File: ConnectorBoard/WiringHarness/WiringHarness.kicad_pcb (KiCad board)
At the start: 2 copper layers, 55 x 30 mm, 16 parts, among them J1 Barrel_Jack, J2 Conn_01x03, J3 Conn_01x03, J4 Conn_02x05_Odd_Even, U1 L7805, U2 L7805

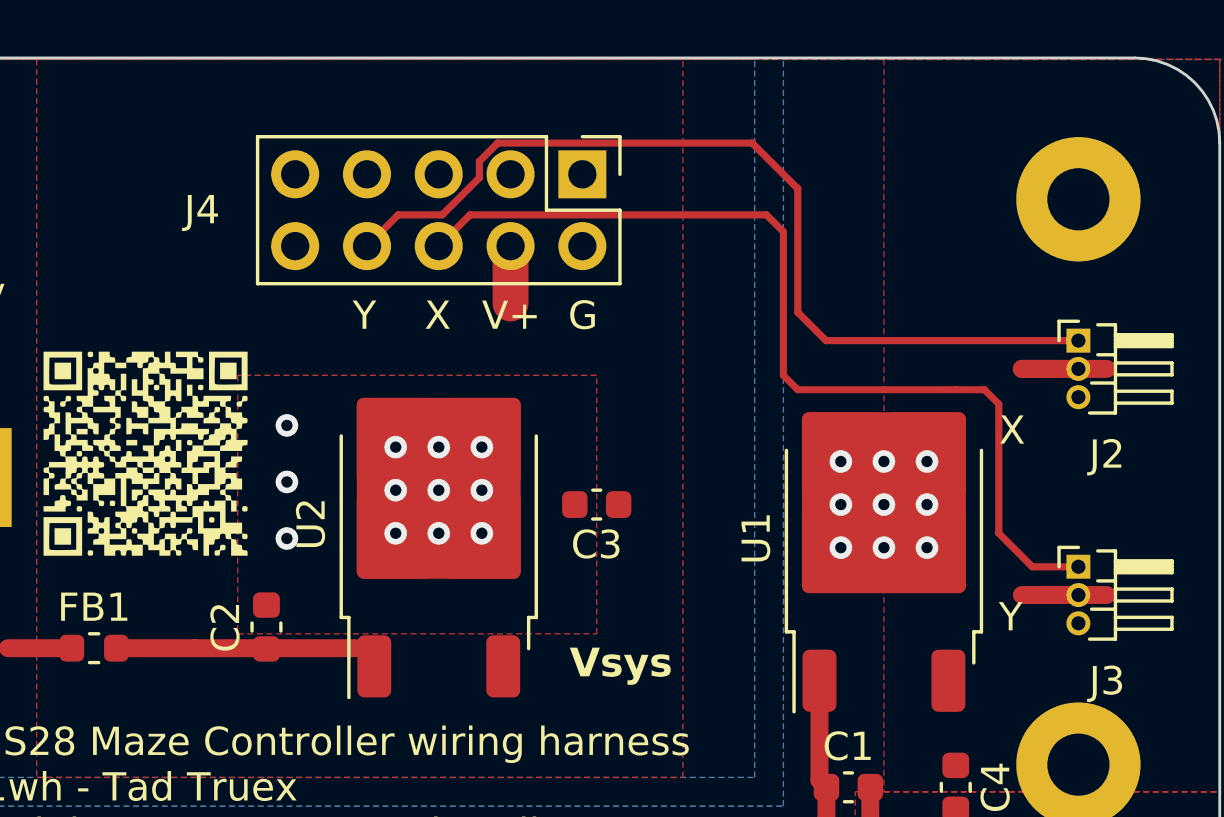
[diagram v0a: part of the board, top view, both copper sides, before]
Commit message: Tweak the connector board a bit.  Rearrange X and Y.  May do more depending on the other board.
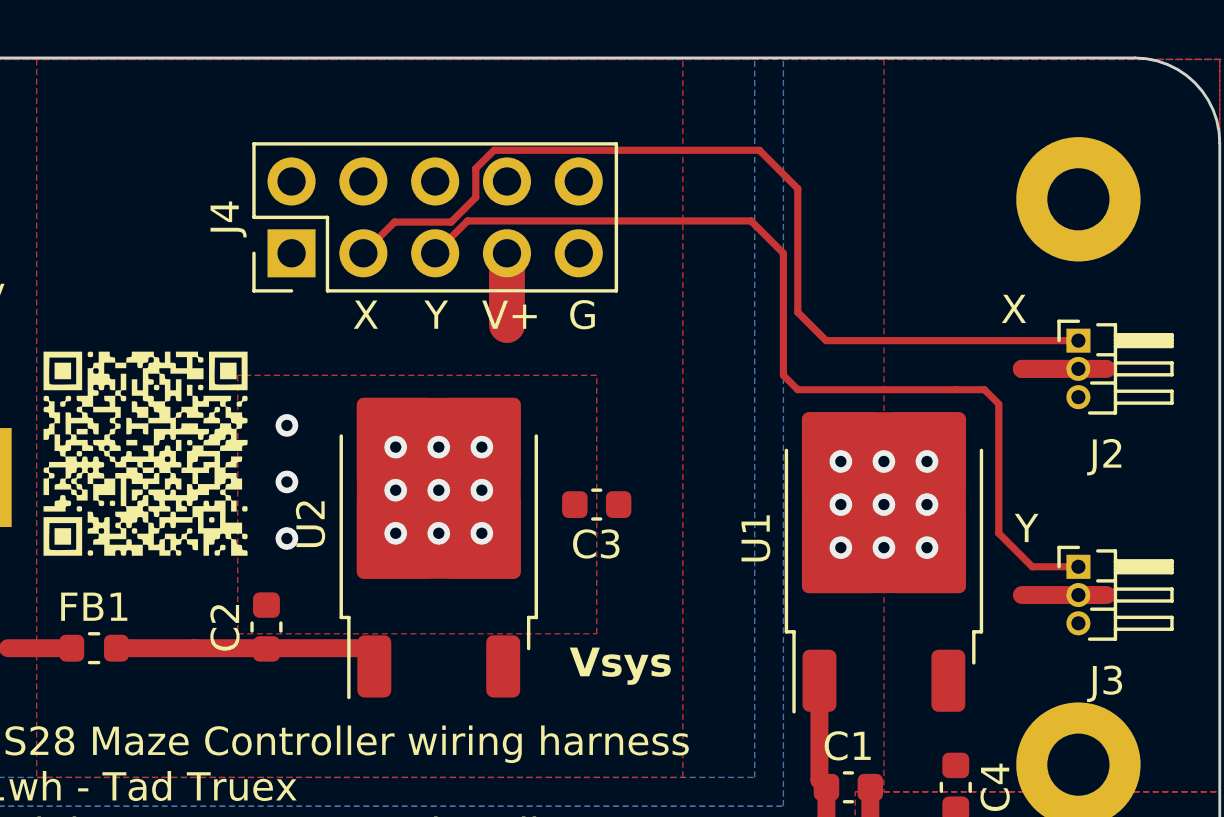
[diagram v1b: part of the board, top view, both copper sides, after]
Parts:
- moved J4 10.7 mm to (177.2, 41.9), turned to 90 degrees
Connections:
- J2 pad 1: /ServoY -> /ServoX
- J3 pad 1: /ServoX -> /ServoY
- J4 pad 2: GND -> unconnected-(J4-Pin_2-Pad2)
- J4 pad 3: unconnected-(J4-Pin_3-Pad3) -> /ServoX
- J4 pad 4: /Vsys -> unconnected-(J4-Pin_4-Pad4)
- J4 pad 5: unconnected-(J4-Pin_5-Pad5) -> /ServoY
- J4 pad 6: /ServoX -> unconnected-(J4-Pin_6-Pad6)
- J4 pad 7: unconnected-(J4-Pin_7-Pad7) -> /Vsys
- J4 pad 8: /ServoY -> unconnected-(J4-Pin_8-Pad8)
- J4 pad 9: unconnected-(J4-Pin_9-Pad9) -> GND
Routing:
- net /ServoX: track 33.9 -> 32.8 mm
- net /ServoY: track 32.5 -> 33.5 mm
- net /Vsys: track 2.03 -> 2.54 mm

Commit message: updates to connector
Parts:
- removed FB1: FerriteBead_Small, Inductor_SMD:L_0603_1608Metric
- removed G***: LOGO, QRCodeLibrary:v0.1wh
- added C5: 1uF, Capacitor_SMD:C_0603_1608Metric, F.Cu at (191.5, 43.0)
- added C6: 1uF, Capacitor_SMD:C_0603_1608Metric, F.Cu at (190.7, 37.0)
- added D1: D_Schottky, Diode_SMD:D_SMA, F.Cu at (170.0, 39.2)
- added J5: Socket, Connector_PinSocket_2.54mm:PinSocket_1x04_P2.54mm_Vertical, F.Cu at (184.6, 28.8)
- added J6: Qwiic, Connector_JST:JST_SH_SM04B-SRSS-TB_1x04-1MP_P1.00mm_Horizontal, F.Cu at (197.0, 32.9)
- added JP1: SolderJumper_3_Bridged12, Jumper:SolderJumper-3_P1.3mm_Bridged12_RoundedPad1.0x1.5mm, F.Cu at (197.3, 39.0)
- J2, J3: footprint Connector_PinHeader_1.00mm:PinHeader_1x03_P1.00mm_Horizontal -> Connector_PinHeader_2.54mm:PinHeader_1x03_P2.54mm_Horizontal
- U2: value L7805 -> TLV75533PDBV; footprint Package_TO_SOT_SMD:TO-252-2 -> Package_TO_SOT_SMD:SOT-23-5
- moved J4 19.5 mm to (187.4, 58.5), turned to -90 degrees
- moved U2 14.2 mm to (190.8, 40.0), turned to 0 degrees
- moved C2 9.81 mm to (186.1, 55.9), turned to 0 degrees
- moved H1 5.00 mm to (205.0, 35.0)
- moved H5 5.00 mm to (160.0, 35.0)
- moved J2 5.00 mm to (205.0, 40.0)
- moved J3 3.00 mm to (205.0, 50.0)
- moved C3 2.79 mm to (185.9, 52.7), turned to 0 degrees
- moved C4 0.66 mm to (200.0, 60.8)
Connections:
- C2 pad 1: /Visol -> /Vsys
- J4 pad 2: unconnected-(J4-Pin_2-Pad2) -> /SCL
- J4 pad 4: unconnected-(J4-Pin_4-Pad4) -> /SDA
- U2 pad 1: /Visol -> /VoutServo
- U2 pad 3: /Vsys -> /VoutServo
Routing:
- net /ServoY: track 33.5 -> 0.00 mm
- net /ServoX: track 32.8 -> 0.00 mm
- net /Visol: track 9.39 -> 0.00 mm
- net /VoutServo: track 8.00 -> 0.00 mm
- net Net-(J6-Pin_2): track 0.00 -> 4.21 mm
- net Net-(JP1-B): track 0.00 -> 4.13 mm
- net GND: track 4.23 -> 7.26 mm, vias 25 -> 4
- net /Vsys: track 2.54 -> 0.20 mm
- net +12V: track 8.03 -> 9.39 mm
- removed copper zone on F.Cu, net +12V
- removed copper zone on F.Cu, net /Vsys
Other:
- board size 55 x 30 mm -> 55 x 35 mm

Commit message: decent candidate for rev 0.5wh
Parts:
- added G***: LOGO, QRCodeLibrary:v0.5wh, F.Cu at (168.5, 60.0)
- added J7: Header, Connector_PinHeader_2.54mm:PinHeader_1x04_P2.54mm_Horizontal, F.Cu at (166.0, 30.0)
- moved C1 14.6 mm to (190.2, 47.8)
- moved C3 13.9 mm to (172.5, 56.5)
- moved C2 13.6 mm to (172.5, 54.2)
- moved D1 11.1 mm to (172.8, 50.0)
- moved C6 6.35 mm to (197.0, 38.0), turned to 0 degrees
- moved H1 5.00 mm to (205.0, 30.0)
- moved H5 5.00 mm to (160.0, 30.0)
- moved J6 4.88 mm to (197.0, 28.0)
- moved C5 3.50 mm to (191.5, 39.5)
- moved JP1 3.50 mm to (197.3, 35.5)
- moved U2 3.50 mm to (190.8, 36.5)
- moved C4 3.09 mm to (198.2, 58.2), turned to 180 degrees
- moved U1 2.65 mm to (196.7, 49.7)
- moved J2 2.52 mm to (205.0, 37.5)
- moved J3 2.52 mm to (205.0, 47.5)
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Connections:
- C1 pad 1: +12V -> /Vsys
- D1 pad 2: +12V -> Net-(D1-A)
- J1 pad 1: +12V -> Net-(D1-A)
- J4 pad 1: unconnected-(J4-Pin_1-Pad1) -> /ServoX
- J4 pad 2: /SCL -> /ServoY
- J4 pad 3: /ServoX -> /SCL
- J4 pad 5: /ServoY -> /D0
- J4 pad 6: unconnected-(J4-Pin_6-Pad6) -> /D1
- U1 pad 1: +12V -> /Vsys
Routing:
- net /SDA: track 0.00 -> 48.0 mm
- net /SCL: track 0.00 -> 42.3 mm
- net /D1: track 0.00 -> 38.6 mm
- net /ServoX: track 0.00 -> 35.1 mm
- net /D0: track 0.00 -> 35.0 mm
- net /ServoY: track 0.00 -> 25.5 mm
- net GND: track 7.26 -> 32.1 mm, vias 4 -> 16
- net +12V: track 9.39 -> 0.00 mm
- net /VoutServo: track 0.00 -> 5.73 mm
- net Net-(D1-A): track 0.00 -> 5.57 mm
- net Net-(JP1-B): track 4.13 -> 6.84 mm
- net /Vsys: track 0.20 -> 2.75 mm
- net Net-(J6-Pin_2): track 4.21 -> 5.50 mm
- added copper zone on F.Cu, net /Vsys
- removed copper zone on F.Cu, net GND
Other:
- board size 55 x 35 mm -> 55 x 40 mm
- board text added: "1 0 V G"
- board text added: "5V"
- board text added: "ENGS28 Maze Controller wiring harness V0.5wh - Tad Truex Copyright 2023, Dartmouth College"
- board text added: "V G D C"
- board text removed: "ENGS28 Maze Controller wiring harness V0.1wh - Tad Truex Copyright 2023, Dartmouth College"
- board text removed: "Vsys"

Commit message: Like 0.5 candidate
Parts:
- J7: footprint Connector_PinHeader_2.54mm:PinHeader_1x04_P2.54mm_Horizontal -> Connector_JST:JST_PH_S4B-PH-K_1x04_P2.00mm_Horizontal
- moved G*** 22.9 mm to (190.0, 52.2)
- moved J7 6.65 mm to (172.5, 31.2), turned to 180 degrees
- moved C3 5.72 mm to (167.5, 59.2), turned to -90 degrees
- moved C2 5.70 mm to (169.8, 59.2), turned to -90 degrees
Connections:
- J7 pad 1: /D1 -> GND
- J7 pad 2: /D0 -> /VoutServo
- J7 pad 3: /VoutServo -> /D0
- J7 pad 4: GND -> /D1
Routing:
- net GND: track 32.1 -> 17.1 mm
- net /Vsys: track 2.75 -> 8.88 mm
- net /D1: track 38.6 -> 37.2 mm
- net /D0: track 35.0 -> 33.8 mm
- added copper zone on F.Cu, net GND
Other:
- board text added: "D0"
- board text added: "D1"
- board text removed: "1 0 V G"

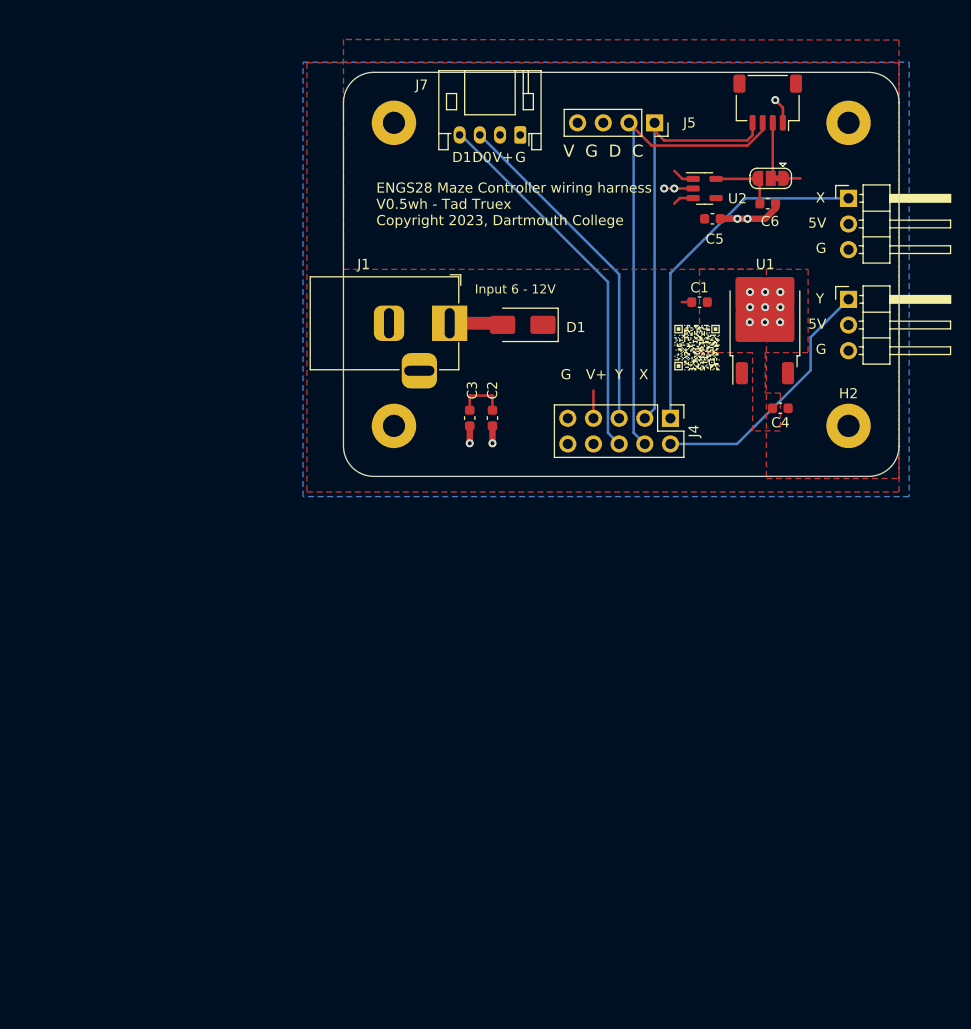
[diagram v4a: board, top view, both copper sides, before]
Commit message: fix step file
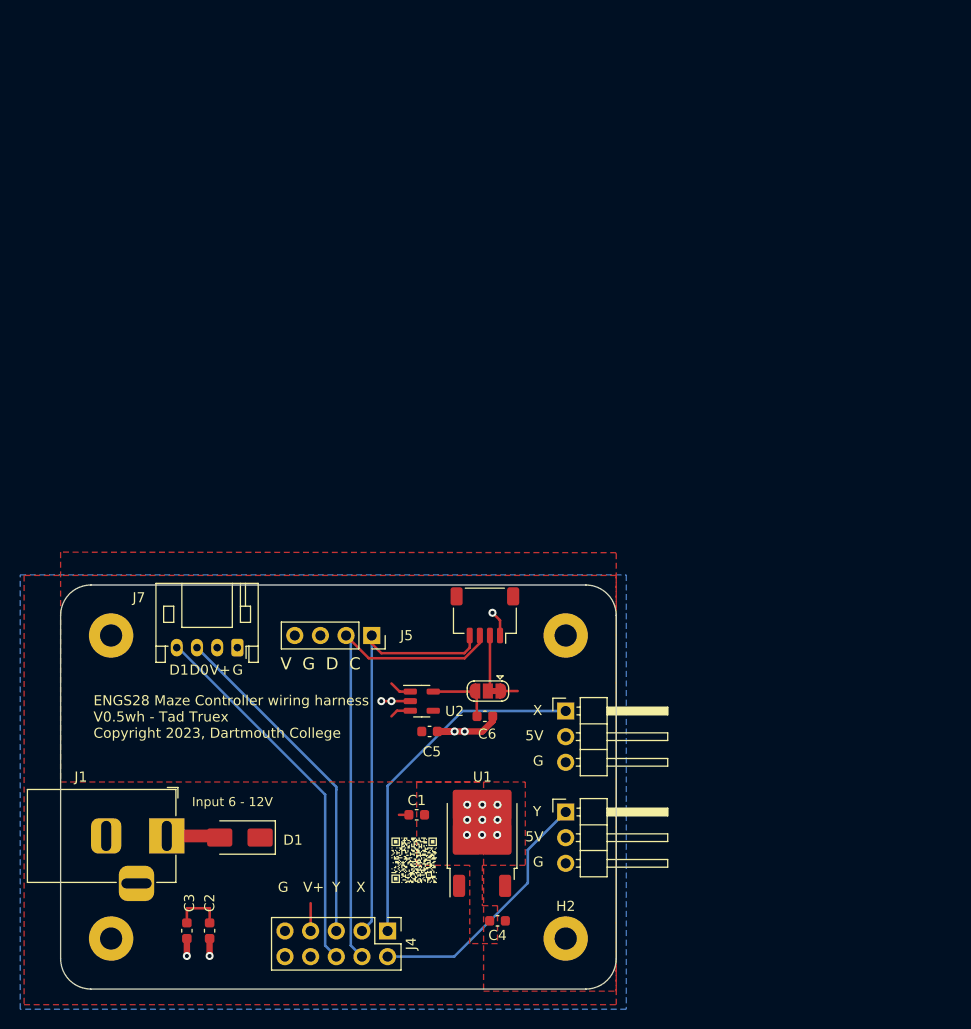
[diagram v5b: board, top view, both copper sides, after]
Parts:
- moved C1 58.0 mm to (162.2, 98.5)
- moved C4 58.0 mm to (170.2, 109.0)
- moved C5 58.0 mm to (163.5, 90.2)
- moved C6 58.0 mm to (169.0, 88.8)
- moved D1 58.0 mm to (144.8, 100.8)
- moved G*** 58.0 mm to (162.0, 103.0)
- moved H1 58.0 mm to (177.0, 80.8)
- moved H2 58.0 mm to (177.0, 110.8)
- moved H3 58.0 mm to (132.0, 110.8)
- moved H5 58.0 mm to (132.0, 80.8)
- moved J1 58.0 mm to (137.5, 100.6)
- moved J4 58.0 mm to (159.4, 110.0)
- moved J5 58.0 mm to (157.8, 80.8)
- moved J6 58.0 mm to (169.0, 78.8)
- moved J7 58.0 mm to (144.5, 82.0)
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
